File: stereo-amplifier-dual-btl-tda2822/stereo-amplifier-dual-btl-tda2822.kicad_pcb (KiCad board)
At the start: 2 copper layers, 50.6 x 54.6 mm, 39 parts, among them J1 SPK L, J2 SPK R, J3 PWR IN, J4 AUX IN, U1 TDA2822, U2 TDA2822

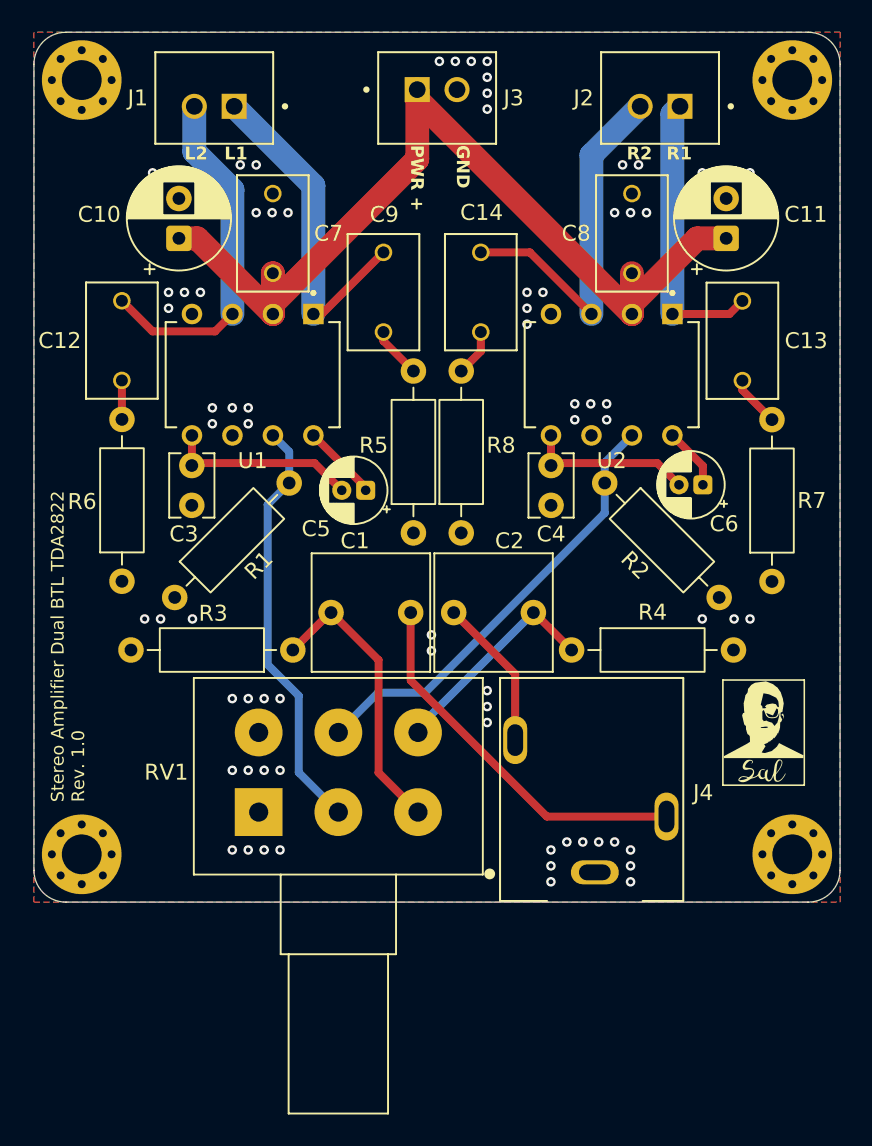
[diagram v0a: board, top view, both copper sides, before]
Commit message: Redesign stereo amplifier PCB for Rev 2.0
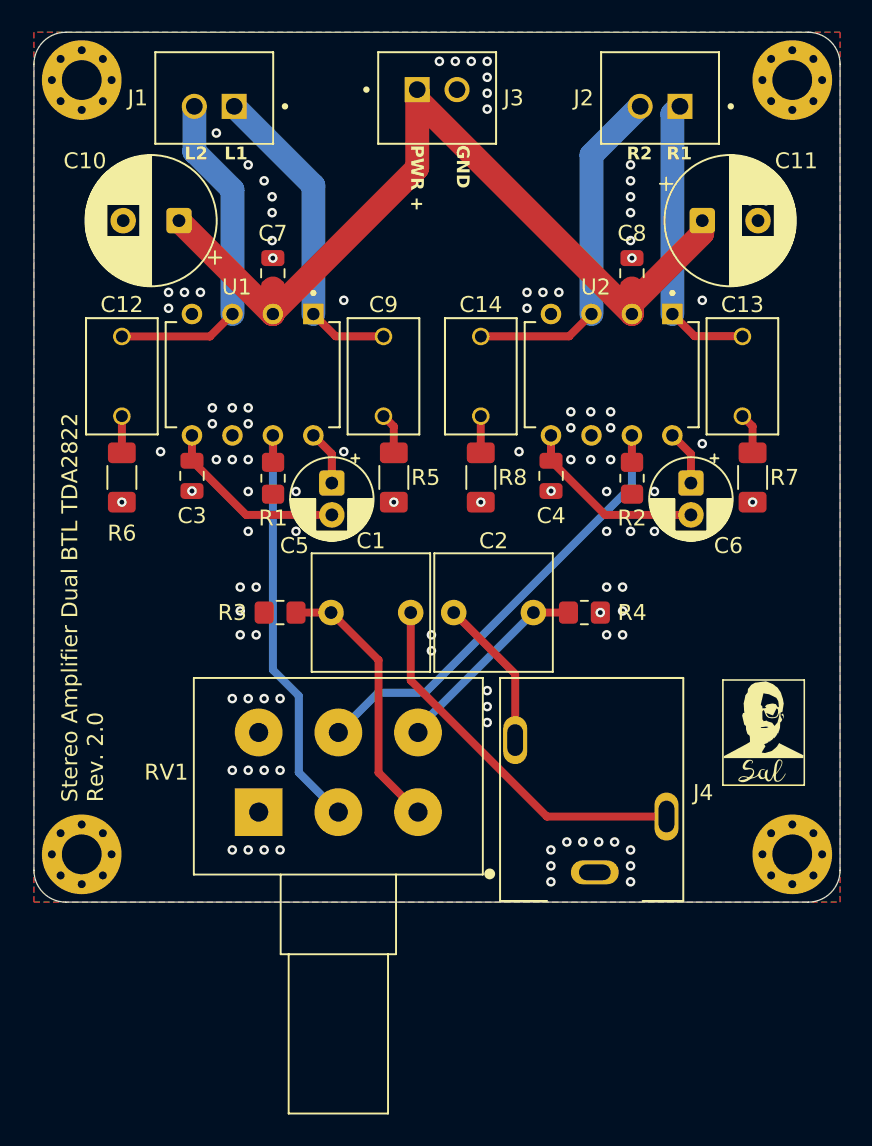
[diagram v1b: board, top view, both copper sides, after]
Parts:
- C1, C2: value 2.2u -> 4.7u
- C10, C11: value 220u -> 470u; footprint Capacitor_THT:CP_Radial_D6.3mm_P2.50mm -> Capacitor_THT:CP_Radial_D8.0mm_P3.50mm
- C3, C4: footprint Capacitor_THT:C_Disc_D3.8mm_W2.6mm_P2.50mm -> Capacitor_SMD:C_0805_2012Metric
- C5, C6: value 10u -> 22u; footprint Capacitor_THT:CP_Radial_D4.0mm_P1.50mm -> Capacitor_THT:CP_Radial_D5.0mm_P2.00mm
- C7, C8: footprint footprints:CAPRR500W50L730T450H950 -> Capacitor_SMD:C_0805_2012Metric
- R1, R2, R3, R4: footprint Resistor_THT:R_Axial_DIN0207_L6.3mm_D2.5mm_P10.16mm_Horizontal -> Resistor_SMD:R_0805_2012Metric_Pad1.20x1.40mm_HandSolder
- R5, R6, R7, R8: footprint Resistor_THT:R_Axial_DIN0207_L6.3mm_D2.5mm_P10.16mm_Horizontal -> Resistor_SMD:R_1206_3216Metric_Pad1.30x1.75mm_HandSolder
- moved R7 6.64 mm to (165.7, 95.1)
- moved R6 6.52 mm to (126.1, 95.1)
- moved C14 5.28 mm to (148.6, 88.8)
- moved C9 5.28 mm to (142.5, 88.8)
- moved R5 3.69 mm to (143.1, 95.1)
- moved R8 3.69 mm to (148.6, 95.1)
- moved C7 2.50 mm to (135.5, 82.3)
- moved C8 2.50 mm to (158.1, 82.3)
- moved R3 2.48 mm to (136.0, 103.6)
- moved R4 2.48 mm to (155.1, 103.6)
- moved C12 2.24 mm to (126.1, 88.8)
- moved C13 2.23 mm to (165.0, 88.8)
- moved C5 2.17 mm to (139.2, 95.5), turned to -90 degrees
- moved C11 1.87 mm to (162.5, 79.0), turned to 0 degrees
- moved C3 1.85 mm to (130.5, 95.0)
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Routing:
- net VCC: track 58.8 -> 56.1 mm
- net RIN: track 28.0 -> 29.7 mm
- net L_PIN8: track 4.80 -> 3.47 mm
- net Net-(C4-Pad2): track 10.6 -> 11.8 mm
- net Net-(C2-Pad2): track 13.9 -> 12.8 mm
- net Net-(C1-Pad2): track 18.2 -> 17.0 mm
- net ROUT2: track 22.8 -> 21.8 mm
- net LOUT1: track 21.1 -> 20.1 mm
- net LOUT2: track 22.2 -> 21.6 mm
- net Net-(C9-Pad1): track 3.23 -> 2.57 mm
- net Net-(C14-Pad1): track 2.96 -> 2.30 mm
- net Net-(C13-Pad1): track 3.22 -> 2.57 mm
- net LIN: track 26.5 -> 27.0 mm
- net GND: vias 83 -> 119
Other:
- board text added: "Stereo Amplifier Dual BTL TDA2822 Rev. 2.0"
- board text removed: "Stereo Amplifier Dual BTL TDA2822 Rev. 1.0"

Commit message: Removed vias in pad from Stereo Amplifier Dual BTL TDA2822
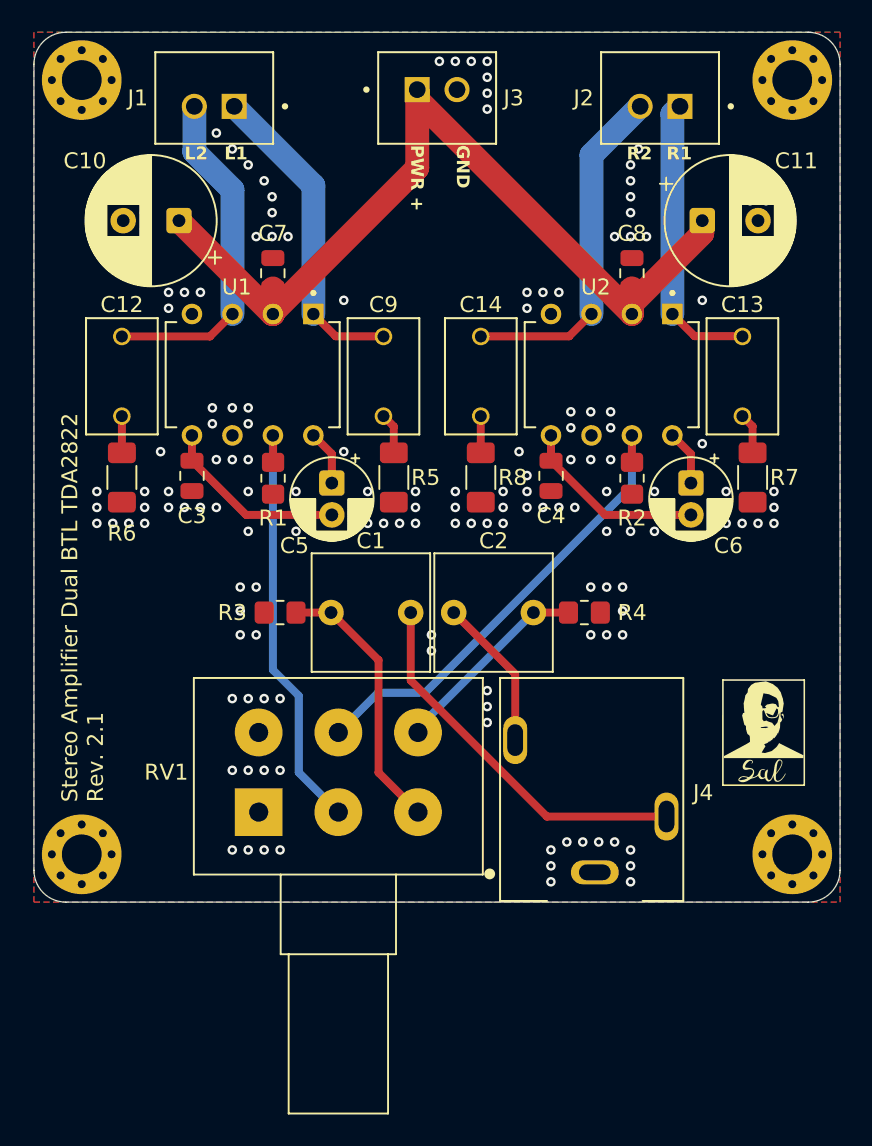
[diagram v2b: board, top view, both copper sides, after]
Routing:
- net GND: vias 119 -> 161
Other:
- board text added: "Stereo Amplifier Dual BTL TDA2822 Rev. 2.1"
- board text removed: "Stereo Amplifier Dual BTL TDA2822 Rev. 2.0"

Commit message: Stereo Amplifier Dual BTL TDA2822 - reorganized project libraries into libs directory
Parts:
- removed the G*** at (166.3, 110.2)
- removed the G*** at (166.2, 113.5)
- removed the G*** at (126.0, 109.6)
- removed the G*** at (126.1, 112.9)
- added G***: LOGO, sal_footprints:SalSig, F.Cu at (166.2, 113.5)
- added G***: LOGO, sal_footprints:SalLogo, F.Cu at (166.3, 110.2)
- added G***: LOGO, sal_footprints:SalSig, B.Cu at (126.1, 112.9)
- added G***: LOGO, sal_footprints:SalLogo, B.Cu at (126.0, 109.6)
- C12, C13, C14, C9: footprint footprints:CAPRR500W50L730T450H950 -> external_footprints:CAPRR500W50L730T450H950
- J1, J2, J3: footprint footprints:JST_B2B-XH-A -> external_footprints:JST_B2B-XH-A
- J4: footprint footprints:CUI_SJ1-3513N -> external_footprints:CUI_SJ1-3513N
- U1, U2: footprint footprints:DIP762W45P254L1092H508Q8 -> external_footprints:DIP762W45P254L1092H508Q8
